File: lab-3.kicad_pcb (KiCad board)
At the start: 4 copper layers, 30.3 x 64.1 mm, 43 parts, among them J1 Conn_SWD, J2 USB_C_Receptacle, J3 Conn_PORT C, J4 Conn_GND, SW1 NRST, SW2 BOOT, SW3 USER, U1 LM66100DCK, U2 LM66100DCK, U3 STM32F405RGTx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

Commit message: Add I2C
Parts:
- added J5: Conn_01x04_Pin, Connector_PinHeader_2.54mm:PinHeader_1x04_P2.54mm_Vertical, F.Cu at (170.5, 88.1)
- added R11: 4.7k, Resistor_SMD:R_0603_1608Metric, F.Cu at (162.5, 89.0)
- added R12: 4.7k, Resistor_SMD:R_0603_1608Metric, F.Cu at (162.5, 87.0)
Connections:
- U3 pad 58: unconnected-(U3-PB6-Pad58) -> /I2C1_SCL
- U3 pad 59: unconnected-(U3-PB7-Pad59) -> /I2C1_SDA
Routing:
- net /I2C1_SDA: track 0.00 -> 19.2 mm
- net /I2C1_SCL: track 0.00 -> 17.7 mm
- net +3.3V: track 24.3 -> 26.6 mm, vias 16 -> 18

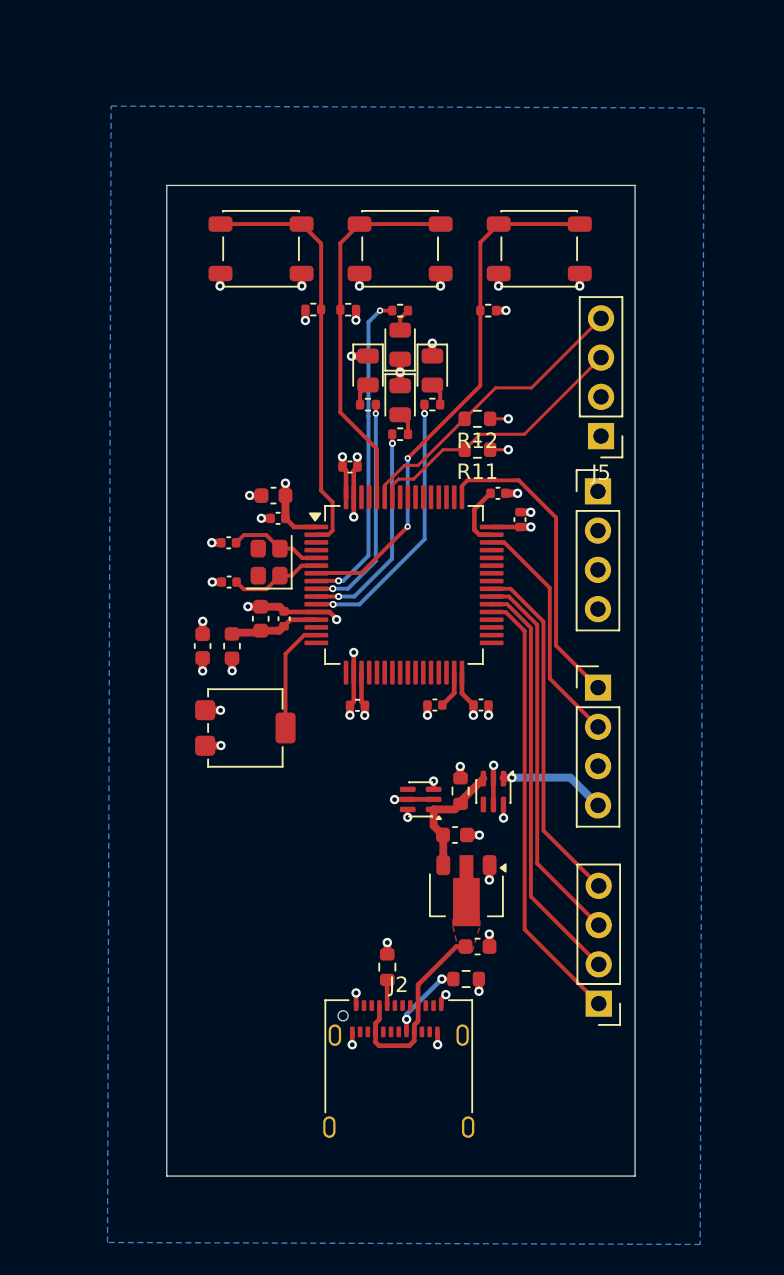
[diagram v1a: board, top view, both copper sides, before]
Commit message: add single 1x24 pin header
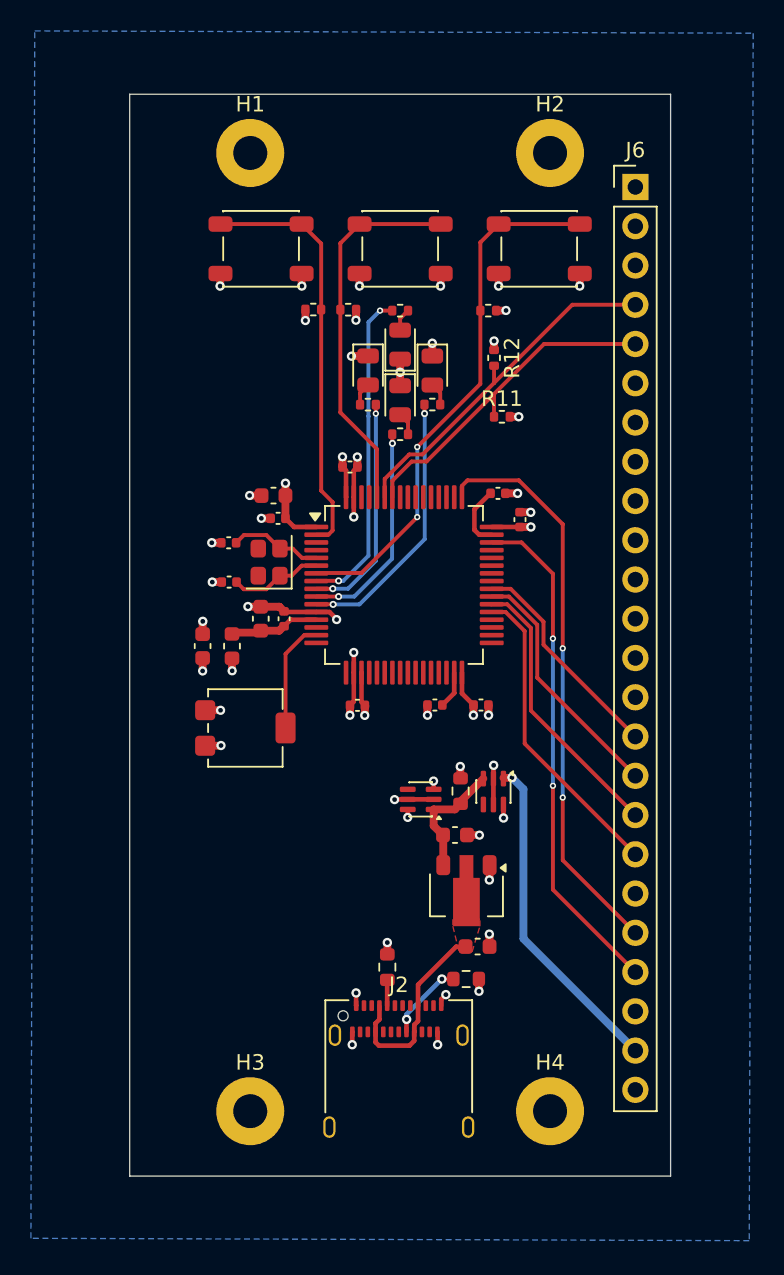
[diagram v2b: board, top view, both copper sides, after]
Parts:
- removed J1: Conn_SWD, Connector_PinHeader_2.54mm:PinHeader_1x04_P2.54mm_Vertical
- removed J3: Conn_PORT C, Connector_PinHeader_2.54mm:PinHeader_1x04_P2.54mm_Vertical
- removed J4: Conn_GND, Connector_PinHeader_2.54mm:PinHeader_1x04_P2.54mm_Vertical
- removed J5: Conn_01x04_Pin, Connector_PinHeader_2.54mm:PinHeader_1x04_P2.54mm_Vertical
- added H1: MountingHole, MountingHole:MountingHole_2.2mm_M2_Pad, F.Cu at (147.8, 69.8)
- added H2: MountingHole, MountingHole:MountingHole_2.2mm_M2_Pad, F.Cu at (167.2, 69.8)
- added H3: MountingHole, MountingHole:MountingHole_2.2mm_M2_Pad, F.Cu at (147.8, 131.8)
- added H4: MountingHole, MountingHole:MountingHole_2.2mm_M2_Pad, F.Cu at (167.2, 131.8)
- added J6: Conn_01x24_Pin, Connector_PinHeader_2.54mm:PinHeader_1x24_P2.54mm_Vertical, F.Cu at (172.7, 72.0)
- R11, R12: footprint Resistor_SMD:R_0603_1608Metric -> Resistor_SMD:R_0402_1005Metric
- moved R12 4.09 mm to (163.6, 83.1), turned to -90 degrees
- moved R11 2.66 mm to (164.1, 86.9), turned to 0 degrees
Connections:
- R11 pad 1: +3.3V -> /I2C1_SCL
- R11 pad 2: /I2C1_SCL -> +3.3V
- U2 pad 1: +3.3V_STLINK -> +3.3V_STLINK_IN
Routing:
- net +3.3V_STLINK_IN: track 0.00 -> 21.5 mm, vias 0 -> 1
- net /SWDIO: track 15.3 -> 32.8 mm, vias 0 -> 2
- net /SWCLK: track 20.1 -> 37.0 mm, vias 0 -> 2
- net /GPIOC_8: track 24.8 -> 16.1 mm
- net /GPIOC_9: track 22.8 -> 14.1 mm
- net /GPIOC_7: track 26.8 -> 18.1 mm
- net /GPIOC_6: track 28.7 -> 20.1 mm
- net +3.3V_STLINK: track 6.87 -> 0.00 mm, vias 1 -> 0
- net /I2C1_SCL: track 17.7 -> 21.9 mm
- net /I2C1_SDA: track 19.2 -> 23.2 mm
- net +3.3V: track 26.6 -> 25.4 mm
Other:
- board size 30.3 x 64.1 mm -> 35 x 70 mm

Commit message: add uart and spi
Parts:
- added R14: 4.7k, Resistor_SMD:R_0402_1005Metric, F.Cu at (163.6, 102.9)
- moved C14 3.14 mm to (165.5, 94.5)
- moved C3 1.93 mm to (163.6, 92.6)
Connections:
- J6 pad 10: /SPI_SCK -> /SPI_MOSI
- J6 pad 12: /SPI_MOSI -> /SPI_SCK
- J6 pad 13: /SPI_CS -> /SPI_NSS
- J6 pad 7: /UART_TX -> /UART_RX
- J6 pad 8: /UART_RX -> /UART_TX
- U3 pad 33: unconnected-(U3-PB12-Pad33) -> /SPI_NSS
- U3 pad 34: unconnected-(U3-PB13-Pad34) -> /SPI_SCK
- U3 pad 35: unconnected-(U3-PB14-Pad35) -> /SPI_MISO
- U3 pad 36: unconnected-(U3-PB15-Pad36) -> /SPI_MOSI
- U3 pad 51: unconnected-(U3-PC10-Pad51) -> /UART_TX
- U3 pad 52: unconnected-(U3-PC11-Pad52) -> /UART_RX
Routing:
- net /UART_RX: track 0.00 -> 15.3 mm
- net /UART_TX: track 0.00 -> 13.6 mm
- net /SPI_MOSI: track 0.00 -> 11.4 mm, vias 0 -> 2
- net /SPI_NSS: track 0.00 -> 11.3 mm, vias 0 -> 2
- net /SPI_MISO: track 0.00 -> 10.6 mm, vias 0 -> 2
- net /SPI_SCK: track 0.00 -> 9.75 mm, vias 0 -> 2
- net Net-(U3-VCAP_2): track 4.06 -> 1.58 mm
- net /SWDIO: track 32.8 -> 32.1 mm
- net /GPIOC_9: track 14.1 -> 14.7 mm
- net /GPIOC_8: track 16.1 -> 16.7 mm
- net /GPIOC_7: track 18.1 -> 18.6 mm
- net +3.3V: track 25.4 -> 25.2 mm, vias 18 -> 19

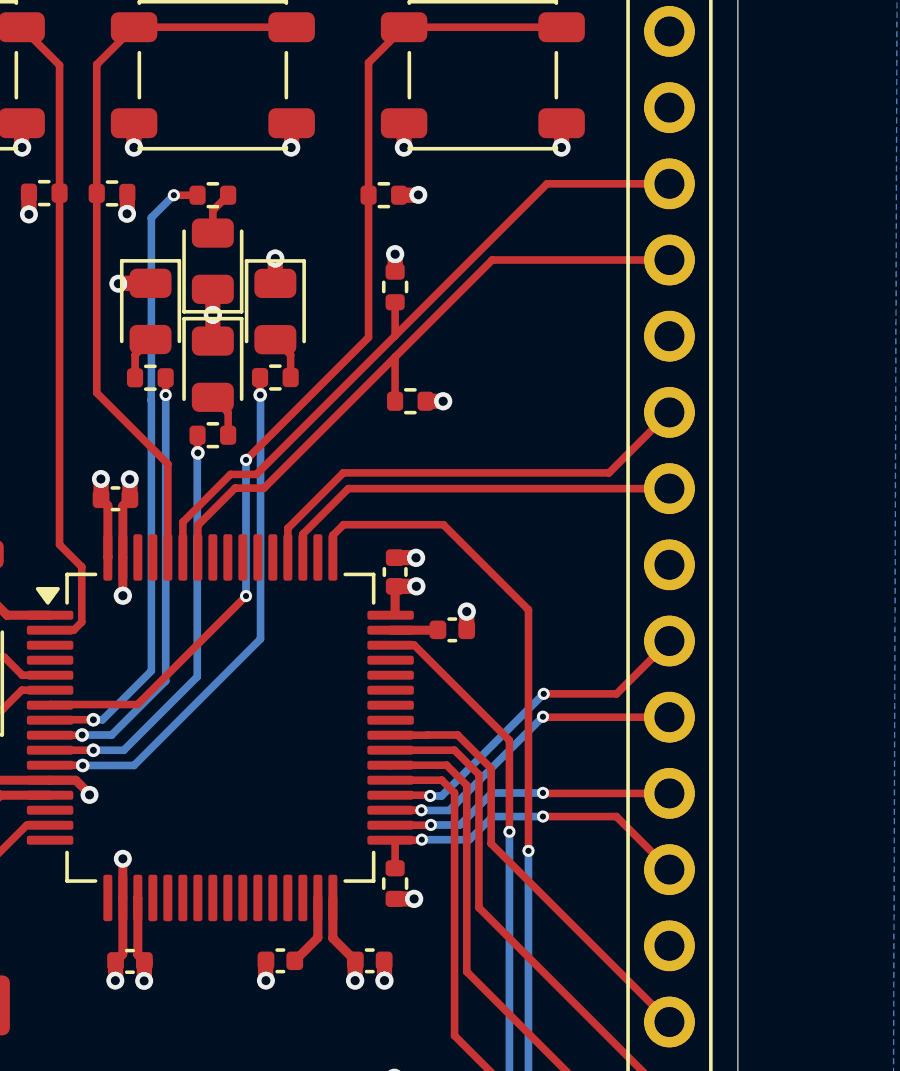
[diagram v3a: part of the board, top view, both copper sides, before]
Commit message: fix i2c and spi trace length
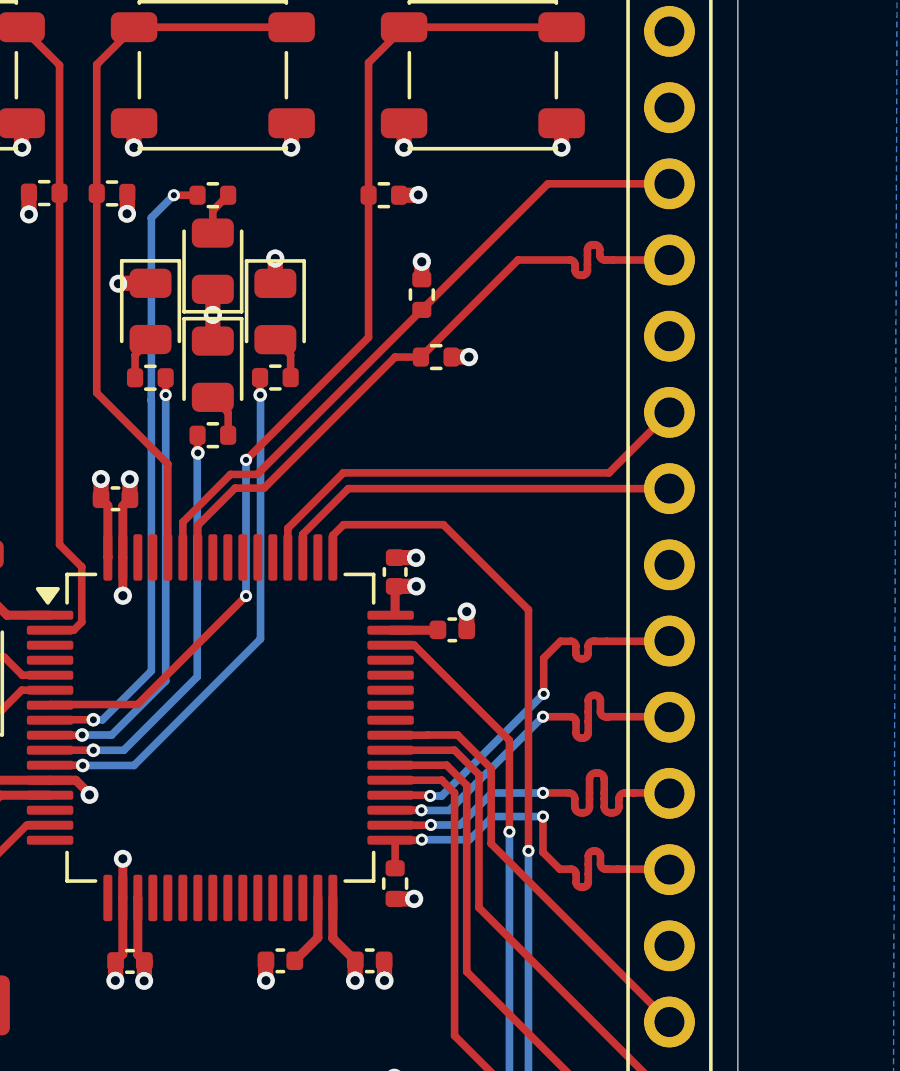
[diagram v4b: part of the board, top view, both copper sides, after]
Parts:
- moved R11 1.71 mm to (164.9, 85.4)
- moved R12 0.92 mm to (164.5, 83.3)
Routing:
- net /SPI_SCK: track 9.75 -> 13.0 mm
- net /SPI_NSS: track 11.3 -> 13.9 mm
- net /SPI_MISO: track 10.6 -> 13.0 mm
- net /SPI_MOSI: track 11.4 -> 13.0 mm
- net /I2C1_SDA: track 23.2 -> 22.1 mm
